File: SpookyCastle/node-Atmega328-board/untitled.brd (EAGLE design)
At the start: 49.9 x 40.5 mm, 24 parts, among them IC2 MEGA48/88/168-AU, J1 RJ11-6PTH

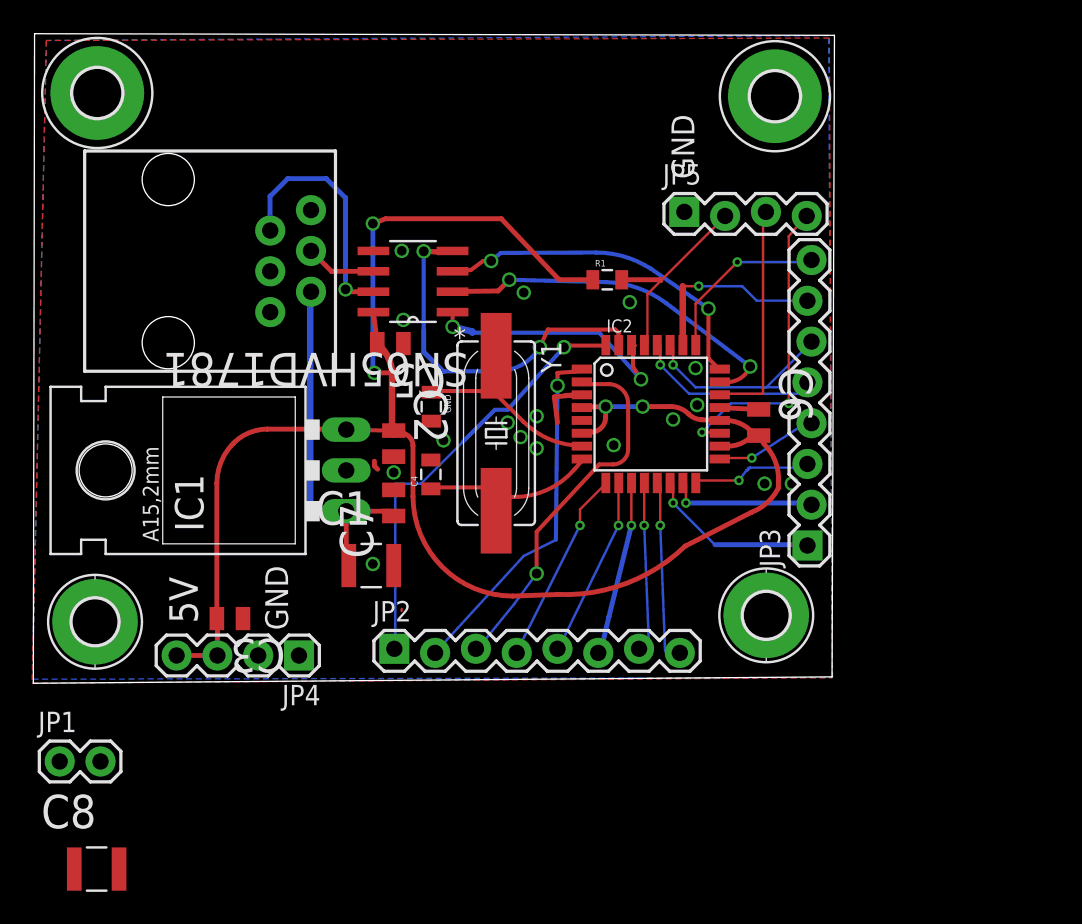
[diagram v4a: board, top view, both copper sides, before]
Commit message: Added a buncha silk to the board.
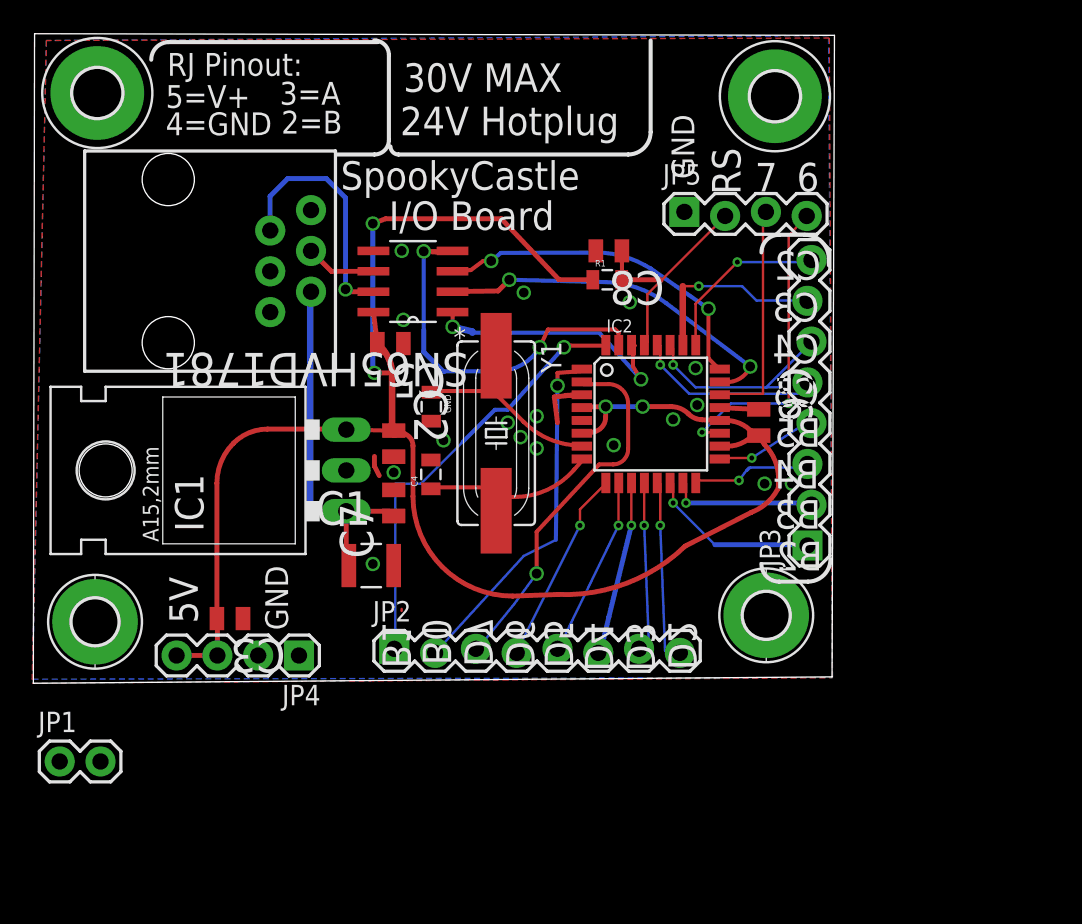
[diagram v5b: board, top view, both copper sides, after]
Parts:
- C8: value 10uF -> 1uF; device Murata_By_element14_Batch_1:CAPC3225X270N -> Murata_By_element14_Batch_1:CAPC2013X135N
- moved C8 50.0 mm to (36.3, 63.1), turned to 180 degrees
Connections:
- net GND: now also C8.2
- net N$22: now also C8.1
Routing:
- net N$22: track 12.6 -> 14.4 mm
- net GND: track 6.39 -> 7.66 mm
- net N$1: track 0.58 -> 0.00 mm
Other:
- board text added: "24V Hotplug"
- board text added: "2=B"
- board text added: "30V MAX"
- board text added: "3=A"
- board text added: "4=GND"
- board text added: "5=V+"
- board text added: "6"
- board text added: "7"
- board text added: "B0"
- board text added: "B1"
- board text added: "B2"
- board text added: "B3"
- board text added: "B4"
- board text added: "B5"
- board text added: "C2"
- board text added: "C3"
- board text added: "C4"
- board text added: "C5"
- board text added: "D2"
- board text added: "D3"
- board text added: "D4"
- board text added: "D5"
- board text added: "D6"
- board text added: "D7"
- board text added: "I/O Board"
- board text added: "RJ Pinout:"
- board text added: "RS"
- board text added: "SpookyCastle"
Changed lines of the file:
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@@
 <text x="14.9" y="43.5" size="1.4224" layer="21" rot="R270">GND</text>
 <text x="40.2" y="71.6" size="1.4224" layer="21" rot="R270">GND</text>
+<text x="49.5" y="61.3" size="1.778" layer="121" rot="MR0">C2</text>
+<text x="49.4" y="58.7" size="1.778" layer="121" rot="MR0">C3</text>
+<text x="49.4" y="56.1" size="1.778" layer="121" rot="MR0">C4</text>
+<text x="49.4" y="53.4" size="1.778" layer="121" rot="MR0">C5</text>
+<text x="49.5" y="50.9" size="1.778" layer="121" rot="MR0">B5</text>
+<text x="49.4" y="48.3" size="1.778" layer="121" rot="MR0">B4</text>
+<text x="49.5" y="45.8" size="1.778" layer="121" rot="MR0">B3</text>
+<text x="49.6" y="43.2" size="1.778" layer="121" rot="MR0">B2</text>
+<text x="22.2" y="37.1" size="1.778" layer="121" rot="MR90">B1</text>
+<text x="24.7" y="37.3" size="1.778" layer="121" rot="MR90">B0</text>
+<text x="27.3" y="37.2" size="1.778" layer="121" rot="MR90">D7</text>
+<text x="29.9" y="37.1" size="1.778" layer="121" rot="MR90">D6</text>
+<text x="32.3" y="37.1" size="1.778" layer="121" rot="MR90">D5</text>
+<text x="34.8" y="36.9" size="1.778" layer="121" rot="MR90">D4</text>
+<text x="37.4" y="36.9" size="1.778" layer="121" rot="MR90">D3</text>
+<text x="40" y="37" size="1.778" layer="121" rot="MR90">D2</text>
+<wire x1="50" y1="62.2" x2="50" y2="62.6" width="0.254" layer="121"/>
+<wire x1="50" y1="62.6" x2="48.5" y2="64.1" width="0.254" layer="121" curve="90"/>
+<wire x1="48.5" y1="64.1" x2="46.9" y2="64.1" width="0.254" layer="121"/>
+<wire x1="46.9" y1="64.1" x2="45.8" y2="63" width="0.254" layer="121" curve="90"/>
+<wire x1="45.8" y1="63" x2="45.8" y2="43.6" width="0.254" layer="122"/>
+<wire x1="45.8" y1="43.6" x2="46.9" y2="42.5" width="0.254" layer="121" curve="90"/>
+<wire x1="46.9" y1="42.5" x2="48.7" y2="42.5" width="0.254" layer="121"/>
+<wire x1="48.7" y1="42.5" x2="50.1" y2="43.9" width="0.254" layer="121" curve="90"/>
+<wire x1="22.7" y1="36.5" x2="22.1" y2="36.5" width="0.254" layer="122"/>
+<wire x1="22.1" y1="36.5" x2="21.1" y2="37.5" width="0.254" layer="122" curve="-90"/>
+<wire x1="21.1" y1="37.5" x2="21.1" y2="39.5" width="0.254" layer="122"/>
+<wire x1="21.1" y1="39.5" x2="22.2" y2="40.6" width="0.254" layer="122" curve="-90"/>
+<wire x1="22.2" y1="40.6" x2="41.3" y2="40.6" width="0.254" layer="122"/>
+<wire x1="41.3" y1="40.6" x2="42.5" y2="39.4" width="0.254" layer="122" curve="-90"/>
+<wire x1="42.5" y1="39.4" x2="42.5" y2="37.9" width="0.254" layer="122"/>
+<wire x1="42.5" y1="37.9" x2="41.3" y2="36.7" width="0.254" layer="122" curve="-90"/>
+<text x="45.4" y="66.8" size="1.778" layer="121">7</text>
+<text x="48" y="66.8" size="1.778" layer="121">6</text>
+<text x="44.5" y="66.6" size="1.778" layer="121" rot="R90">RS</text>
+<text x="8.8" y="74" size="1.4224" layer="121">RJ Pinout:</text>
+<text x="8.7" y="72" size="1.4224" layer="121">5=V+</text>
+<text x="8.7" y="70.3" size="1.4224" layer="121">4=GND</text>
+<text x="15.8" y="72.2" size="1.4224" layer="121">3=A</text>
+<text x="15.9" y="70.4" size="1.4224" layer="121">2=B</text>
+<text x="23.5" y="73" size="1.778" layer="121">30V MAX</text>
+<text x="23.3" y="70.3" size="1.778" layer="121">24V Hotplug</text>
+<wire x1="19.3" y1="69.1" x2="21.7" y2="69.1" width="0.254" layer="121"/>
+<wire x1="21.7" y1="69.1" x2="22.6" y2="70" width="0.254" layer="121" curve="90"/>
+<wire x1="22.6" y1="70" x2="22.6" y2="75.3" width="0.254" layer="121"/>
+<wire x1="22.6" y1="75.3" x2="21.7" y2="76.2" width="0.254" layer="121" curve="90"/>
+<wire x1="22.7" y1="69.6" x2="23.2" y2="69.1" width="0.254" layer="121" curve="90"/>
+<wire x1="23.2" y1="69.1" x2="37.5" y2="69.1" width="0.254" layer="121"/>
+<wire x1="37.5" y1="69.1" x2="38.9" y2="70.5" width="0.254" layer="121" curve="90"/>
+<wire x1="38.9" y1="70.5" x2="38.9" y2="76.2" width="0.254" layer="121"/>
+<wire x1="21.9" y1="76.1" x2="8.9" y2="76.1" width="0.254" layer="121"/>
+<wire x1="8.9" y1="76.1" x2="7.8" y2="75" width="0.254" layer="121" curve="90"/>
+<text x="19.6" y="66.9" size="1.778" layer="121">SpookyCastle</text>
+<text x="22.6" y="64.4" size="1.778" layer="121">I/O Board</text>
 </plain>
 <attributes>
@@
 </element>
 <element name="R1" library="SparkFun - Copy" package="0805" value="4.7k" x="36.2" y="61.3"/>
-<element name="C8" library="Murata_By_element14_Batch_1" package="CAPC3225X270N" value="10uF" x="4.4" y="24.6">
-<attribute name="OC_NEWARK" value="24R2634" x="4.4" y="24.6" size="1.778" layer="27" display="off"/>
-<attribute name="TOLERANCE" value="±10%" x="4.4" y="24.6" size="1.778" layer="27" display="off"/>
-<attribute name="MPN" value="GRM32ER7YA106KA12L" x="4.4" y="24.6" size="1.778" layer="27" display="off"/>
-<attribute name="SUPPLIER" value="Murata" x="4.4" y="24.6" size="1.778" layer="27" display="off"/>
-<attribute name="VOLTAGERATING" value="35V" x="4.4" y="24.6" size="1.778" layer="27" display="off"/>
-<attribute name="OC_FARNELL" value="1735537" x="4.4" y="24.6" size="1.778" layer="27" display="off"/>
-<attribute name="VALUE" value="10uF" x="4.4" y="24.6" size="1.778" layer="27" display="off"/>
+<element name="C8" library="Murata_By_element14_Batch_1" package="CAPC2013X135N" value="1uF" x="36.3" y="63.1" rot="R180">
+<attribute name="OC_NEWARK" value="24R6342" x="36.3" y="63.1" size="1.778" layer="27" rot="R180" display="off"/>
+<attribute name="TOLERANCE" value="±10%" x="36.3" y="63.1" size="1.778" layer="27" rot="R180" display="off"/>
+<attribute name="MPN" value="GRM21BR71H105KA12L " x="36.3" y="63.1" size="1.778" layer="27" rot="R180" display="off"/>
+<attribute name="SUPPLIER" value="Murata" x="36.3" y="63.1" size="1.778" layer="27" rot="R180" display="off"/>
+<attribute name="VOLTAGERATING" value="50V" x="36.3" y="63.1" size="1.778" layer="27" rot="R180" display="off"/>
+<attribute name="OC_FARNELL" value="1735541" x="36.3" y="63.1" size="1.778" layer="27" rot="R180" display="off"/>
+<attribute name="VALUE" value="1uF" x="36.3" y="63.1" size="1.778" layer="27" rot="R180" display="off"/>
 </element>
 </elements>
@@
 <wire x1="37.1" y1="61.3" x2="39.5" y2="61.3" width="0.3048" layer="1"/>
 <wire x1="39.5" y1="61.3" x2="39.55" y2="61.25" width="0.3048" layer="1"/>
+<contactref element="C8" pad="1"/>
+<wire x1="37.1" y1="61.3" x2="37.1128" y2="61.3" width="0.254" layer="1"/>
+<wire x1="37.1128" y1="61.3" x2="37.1128" y2="63.1" width="0.254" layer="1"/>
 </signal>
 <signal name="N$4">
@@
 <via x="26" y="51.3" extent="1-16" drill="0.6" diameter="0.3048" shape="octagon"/>
 <via x="41.7" y="55.8" extent="1-16" drill="0.6" diameter="0.3048" shape="octagon"/>
+<wire x1="21.7" y1="50.3" x2="21.7" y2="49.7" width="0.3048" layer="1"/>
+<wire x1="21.7" y1="49.7" x2="22" y2="49.1" width="0.3048" layer="1"/>
+<contactref element="C8" pad="2"/>
 </signal>
 <signal name="VEXTERN" class="1">
@@
 <wire x1="15.2" y1="64.375" x2="15.21" y2="64.365" width="0.3048" layer="16"/>
 </signal>
-<signal name="N$1">
-<wire x1="21.7" y1="50" x2="21.7" y2="49.7" width="0.3048" layer="1"/>
-<wire x1="21.7" y1="49.7" x2="21.9" y2="49.5" width="0.3048" layer="1"/>
-</signal>
 </signals>

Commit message: Updated board and spec pdf. PDF is all bold due to what I think is an OpenOffice bug.
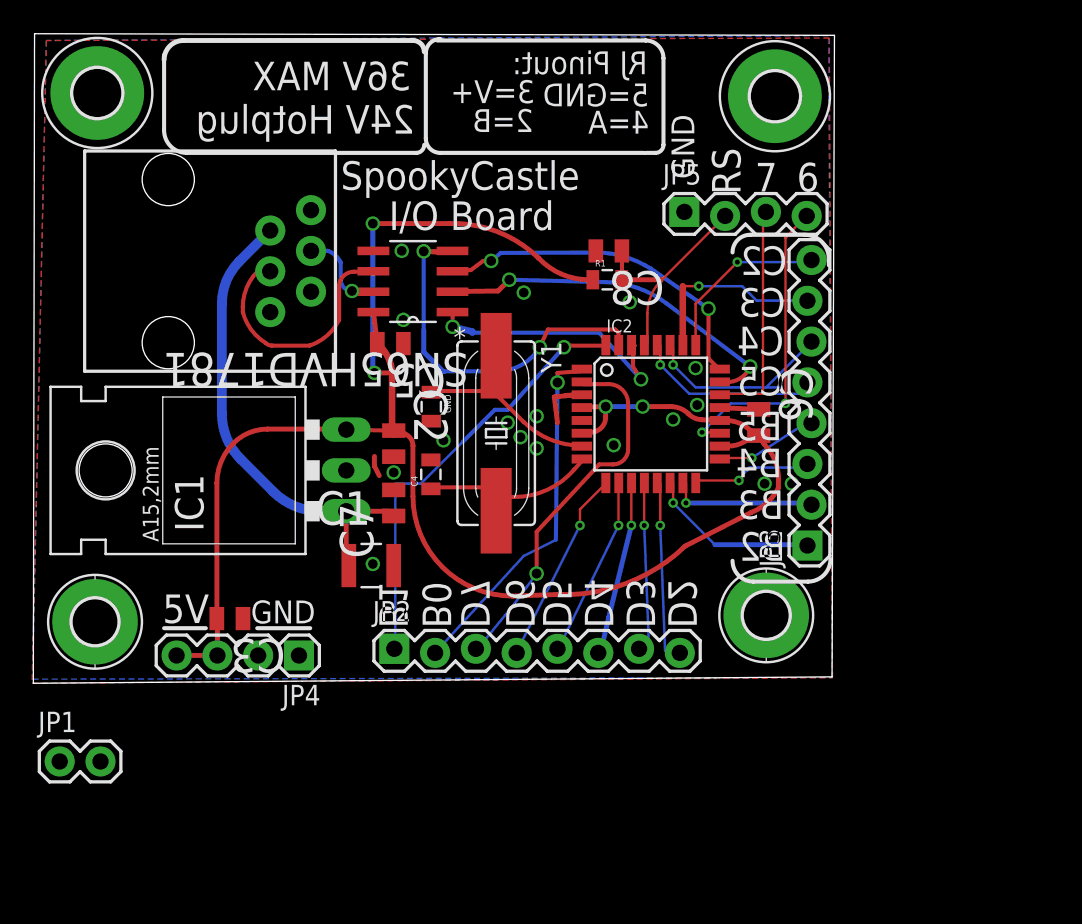
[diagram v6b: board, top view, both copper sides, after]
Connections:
- net A: now also J1.4; no longer J1.3
- net B: now also J1.3; no longer J1.2
- net GND: now also J1.5; no longer J1.4
- net VEXTERN: now also J1.2; no longer J1.5
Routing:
- net A: track 4.41 -> 15.7 mm
- net B: track 15.3 -> 5.55 mm
- net VEXTERN: track 22.4 -> 29.6 mm
- net VCC: track 112.2 -> 111.2 mm
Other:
- board text added: "36V MAX"
- board text added: "3=V+"
- board text added: "4=A"
- board text added: "5=GND"
- board text removed: "30V MAX"
- board text removed: "3=A"
- board text removed: "4=GND"
- board text removed: "5=V+"

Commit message: Fix critical silk error(Text on wrong side) Add HTML version of the spec since OO is outputting all bold PDFs
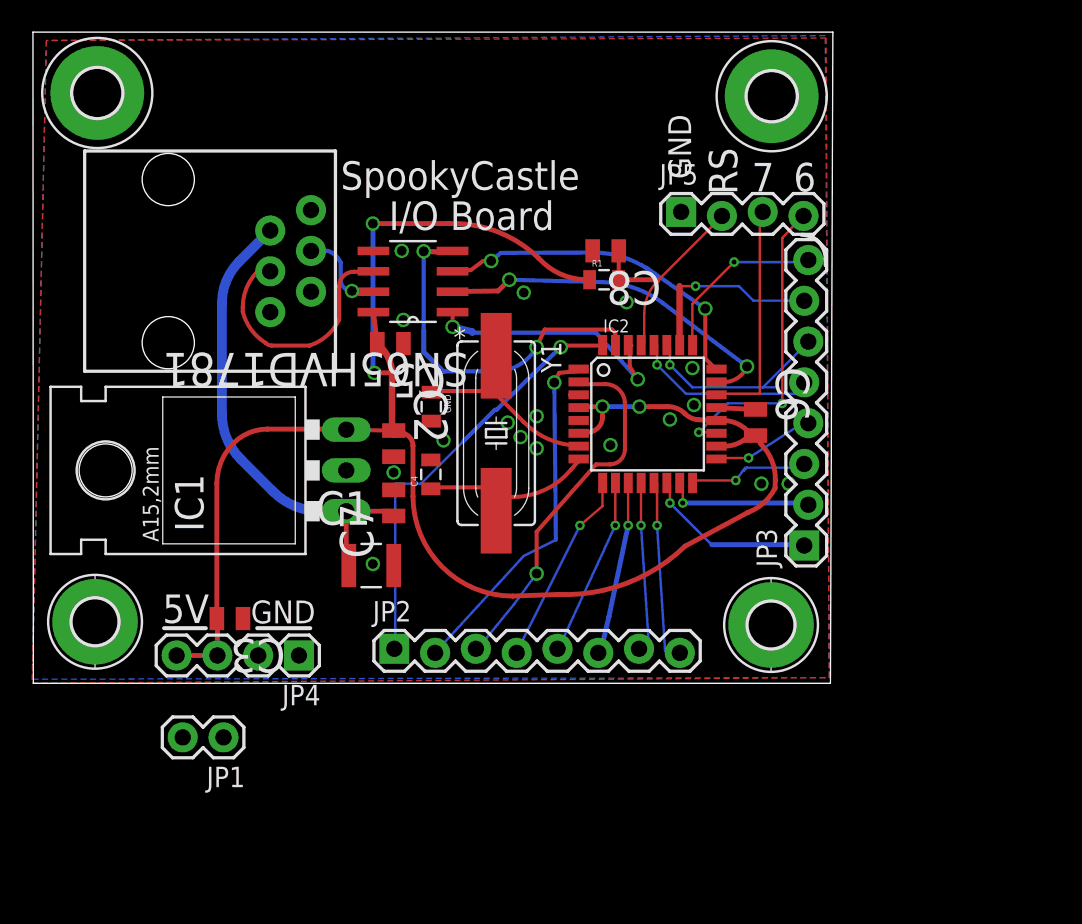
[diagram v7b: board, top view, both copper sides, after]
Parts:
- moved JP1 10.3 mm to (12.3, 32.8), turned to 180 degrees
- moved H4 0.67 mm to (46.4, 39.8)
- moved H2 0.20 mm to (46.4, 72.7)
- moved IC2 0.20 mm to (38.7, 52.9)
- moved JP3 0.20 mm to (48.6, 44.7)
- moved JP5 0.20 mm to (40.8, 65.4)
- moved R1 0.20 mm to (36.0, 61.3)
- moved C6 0.20 mm to (45.4, 52.4)
- moved C8 0.20 mm to (36.1, 63.1)
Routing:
- net GND: track 7.53 -> 2.95 mm
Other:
- board size 49.9 x 40.5 mm -> 49.8 x 40.6 mm
- board text added: "MISO"
- board text added: "MOSI"
- board text added: "SCK"
- board text added: "SCL"
- board text added: "SDA"

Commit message: Updated the spookycastle board to use screw terminals since the spec no longer requires rj11
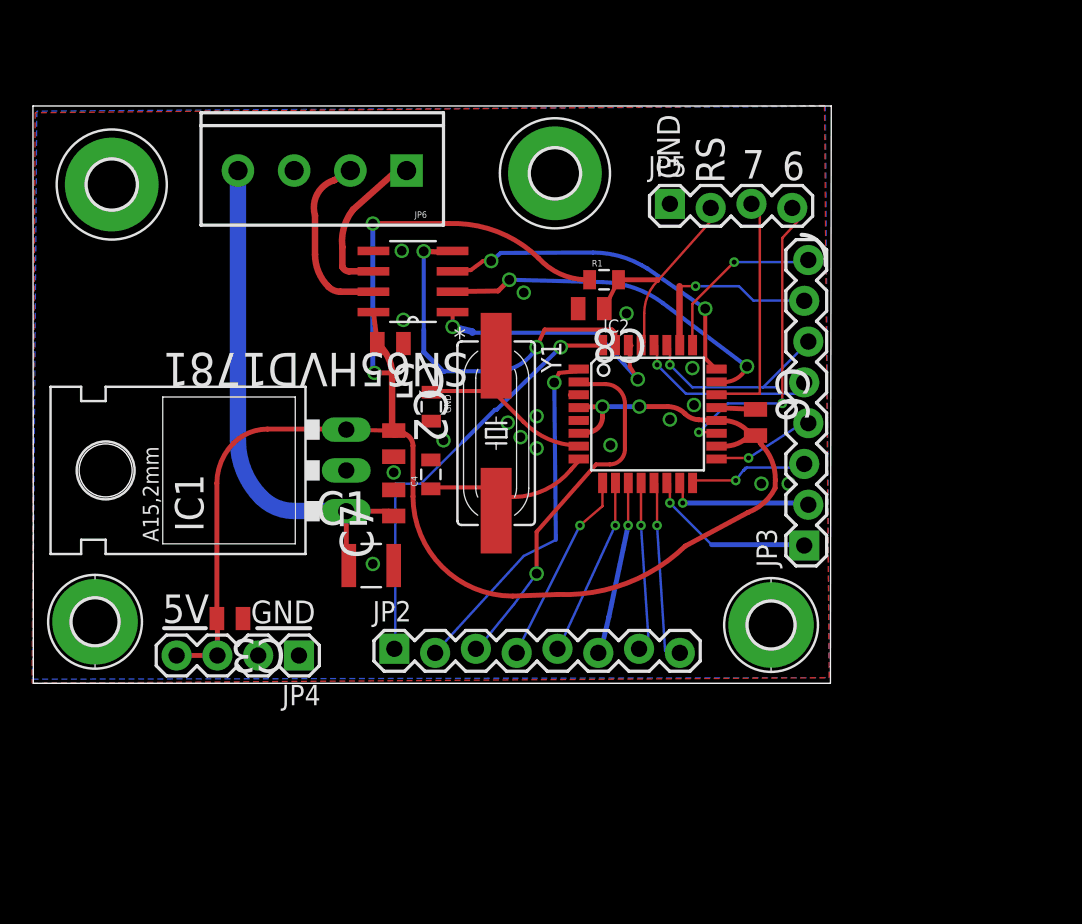
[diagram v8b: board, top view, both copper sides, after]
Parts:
- removed J1: RJ11-6PTH, SparkFun - Copy:RJ11-6
- removed JP1: (no value), SparkFun - Copy:1X02
- added JP6: (no value), SparkFun - Copy:SCREWTERMINAL-3.5MM-4
- moved H2 14.3 mm to (32.9, 67.9)
- moved H1 5.77 mm to (5.34, 67.2)
- moved C8 3.71 mm to (35.2, 59.5)
- moved JP5 0.86 mm to (40.1, 65.9)
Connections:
- net A: now also JP6.1; no longer J1.4
- net B: now also JP6.2; no longer J1.3
- net GND: now also JP6.3; no longer J1.5
- net VEXTERN: now also JP6.4; no longer J1.2
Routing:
- net A: track 15.7 -> 9.94 mm
- net B: track 5.55 -> 11.1 mm, vias 1 -> 0
- net VEXTERN: track 29.6 -> 32.6 mm
- net P19: track 19.3 -> 20.0 mm
- net P22: track 14.1 -> 14.7 mm
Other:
- board size 49.8 x 40.6 mm -> 49.7 x 36 mm
- board text removed: "24V Hotplug"
- board text removed: "2=B"
- board text removed: "36V MAX"
- board text removed: "3=V+"
- board text removed: "4=A"
- board text removed: "5=GND"
- board text removed: "I/O Board"
- board text removed: "RJ Pinout:"
- board text removed: "SpookyCastle"
